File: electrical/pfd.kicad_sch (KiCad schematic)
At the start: 12 parts

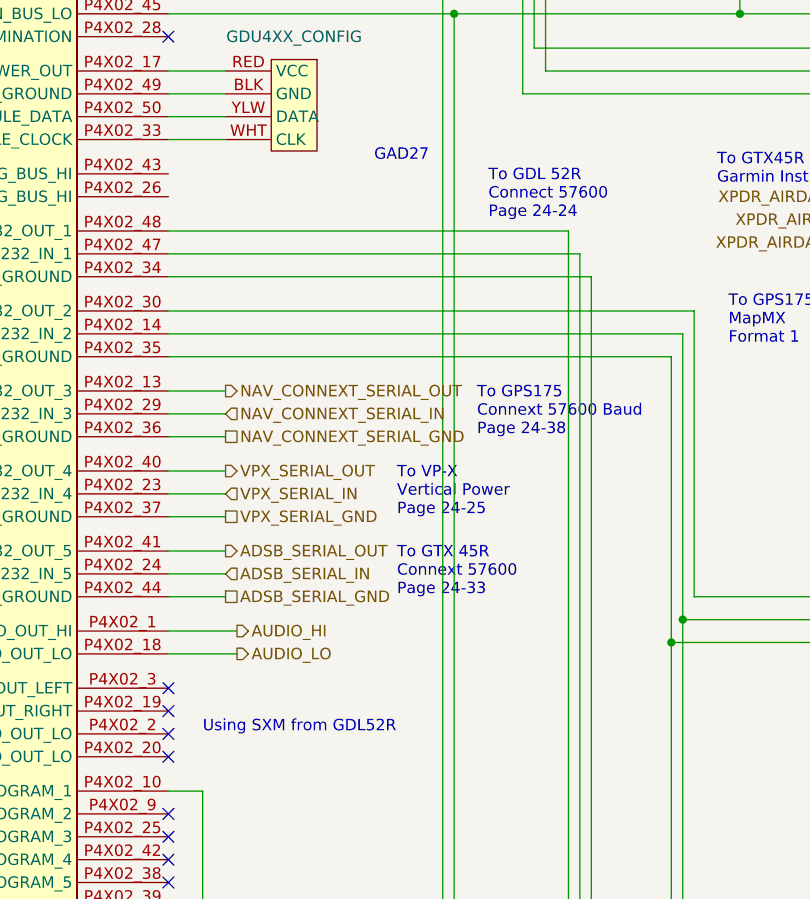
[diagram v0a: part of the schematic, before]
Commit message: Converted to breakers w/GAD 27 instead of VP-X.
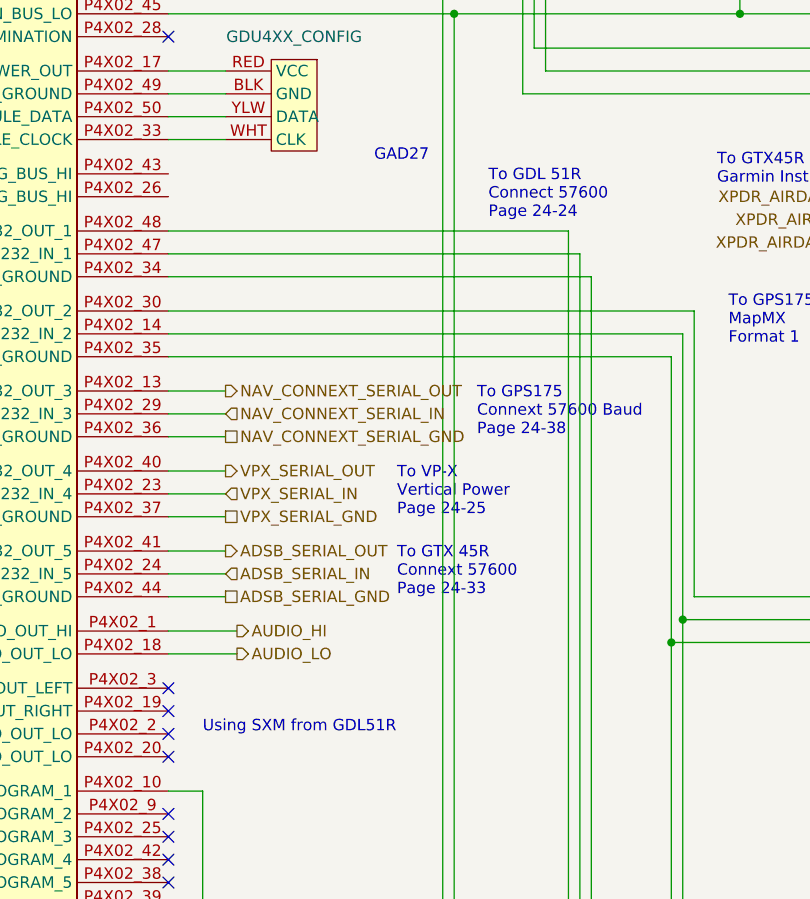
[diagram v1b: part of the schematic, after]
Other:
- note added: "To GDL 51R Connect 57600 Page 24-24"
- note added: "Using SXM from GDL51R"
- note removed: "To GDL 52R Connect 57600 Page 24-24"
- note removed: "Using SXM from GDL52R"
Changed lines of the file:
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@@
     (title "PFD & ADAHRS")
     (date "2024-02-13")
-    (rev "0.9.1")
+    (rev "1.0")
     (company "N915SN Angry Bird")
+    (comment 1 "w/Breakers")
   )
   (junction (at 151.13 212.09) (diameter 0) (color 0 0 0 0)
@@
     (effects (font (size 1.27 1.27)) (justify left bottom))
   )
-  (text "Using SXM from GDL52R" (at 66.04 142.24 0)
+  (text "Using SXM from GDL51R" (at 66.04 142.24 0)
     (effects (font (size 1.27 1.27)) (justify left bottom))
   )
@@
     (effects (font (size 1.27 1.27)) (justify left bottom))
   )
-  (text "To GDL 52R\nConnect 57600\nPage 24-24" (at 97.79 85.09 0)
-    (effects (font (size 1.27 1.27)) (justify left bottom))
-  )
+  (text "To GDL 51R\nConnect 57600\nPage 24-24" (at 97.79 85.09 0)
+    (effects (font (size 1.27 1.27)) (justify left bottom))
+  )

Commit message: Unknown set of changes. Didn't spent time to look
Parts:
- added GHA15_USB: USB_A, symbol Connector:USB_A
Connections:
- net at GHA15.10 (USBO_DM): now also GHA15_USB.2 (D-)
- net at GHA15.19 (USB_VBUS): now also GHA15_USB.1 (VBUS)
- net at GHA15.20 (SIGNAL_GROUND): now also GHA15_USB.4 (GND), GHA15_USB.5 (Shield)
- net at GHA15.9 (USBO_DP): now also GHA15_USB.3 (D+)
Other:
- moved on the sheet: G5, GHA15

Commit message: Interim check-in. Not sure what I was doing.
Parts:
- removed UAT_ANT: Antenna, symbol Device:Antenna
- renumbered GDL52R to GDL51R
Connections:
- net VPX_SERIAL_GND: no longer names the net of GDU450.P4X02_37 (SIGNAL_GROUND)
- net VPX_SERIAL_IN: no longer names the net of GDU450.P4X02_23 (RS-232_IN_4)
- net VPX_SERIAL_OUT: no longer names the net of GDU450.P4X02_40 (RS-232_OUT_4)
- no-connect marks 16 -> 18
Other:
- note removed: "To VP-X Vertical Power Page 24-25"
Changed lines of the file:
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@@
   )
   (no_connect (at 62.23 151.13))
+  (no_connect (at 63.5 234.95))
   (no_connect (at 163.83 200.66))
   (no_connect (at 154.94 35.56))
@@
   (no_connect (at 62.23 139.7))
   (no_connect (at 157.48 160.02))
+  (no_connect (at 63.5 229.87))
   (no_connect (at 62.23 137.16))
   (no_connect (at 62.23 142.24))
@@
     (stroke (width 0) (type default))
   )
-  (wire (pts (xy 63.5 234.95) (xy 64.77 234.95))
-    (stroke (width 0) (type default))
-  )
   (wire (pts (xy 109.22 91.44) (xy 109.22 208.28))
     (stroke (width 0) (type default))
@@
     (stroke (width 0) (type default))
   )
-  (wire (pts (xy 62.23 113.03) (xy 68.58 113.03))
-    (stroke (width 0) (type default))
-  )
   (wire (pts (xy 133.35 168.91) (xy 133.35 195.58))
     (stroke (width 0) (type default))
@@
     (stroke (width 0) (type default))
   )
-  (wire (pts (xy 62.23 118.11) (xy 68.58 118.11))
-    (stroke (width 0) (type default))
-  )
   (wire (pts (xy 62.23 88.9) (xy 107.95 88.9))
     (stroke (width 0) (type default))
@@
     (stroke (width 0) (type default))
   )
-  (wire (pts (xy 62.23 115.57) (xy 68.58 115.57))
-    (stroke (width 0) (type default))
-  )
   (wire (pts (xy 92.71 59.69) (xy 124.46 59.69))
     (stroke (width 0) (type default))
@@
     (stroke (width 0) (type default))
   )
-  (text "To VP-X\nVertical Power\nPage 24-25" (at 87.63 118.11 0)
-    (effects (font (size 1.27 1.27)) (justify left bottom))
+  (text_box "J251\n1 CAN H\n2 CAN L\n4 RS-232 RX-1\n5 RS-232 TX-1\n6 Ground\n7 Power 1\n8 Power 2\n9 Ground"
+    (at 185.42 116.84 0) (size 18.415 19.685)
+    (stroke (width 0) (type default))
+    (fill (type none))
+    (effects (font (size 1.27 1.27)) (justify left top))
+  )
+  (text_box "J4X01 from Zlin\n4 RS-232 RX\n5 RS-232 TX\n6 Signal Gnd"
+    (at 74.295 13.335 0) (size 17.78 9.525)
+    (stroke (width 0) (type default))
+    (fill (type none))
+    (effects (font (size 1.27 1.27)) (justify left top))
+  )
+  (text_box "J252\n 1 OAT Power\n 2 OAT High\n 3 OAT Low\n 9 RS-232 TX 3\n10 RS0232 RX 3\n11 Ground\n"
+    (at 122.555 108.585 0) (size 18.415 15.875)
+    (stroke (width 0) (type default))
+    (fill (type none))
+    (effects (font (size 1.27 1.27)) (justify left top))
+  )
+  (text_box "GDU\nRS232 1 Connext 57600\nRS232 2 Connext 57600\nRS232 3 None\nRS232 4 Garmin Instrument Data\nRS232 5 None\n\nTransponder\nRS232 2 ADS-B+ GPS Format 1\nRS232 3 Connect Format 1\nRS232 4 None"
+    (at -38.735 67.31 0) (size 34.925 24.13)
+    (stroke (width 0) (type default))
+    (fill (type none))
+    (effects (font (size 1.27 1.27)) (justify left top))
+  )
+  (text_box "J4X02 from Zlin\n 3 Stereo Out Left\n 6 Do not use\n10 CDU System ID 1\n14 RS-232 IN\n16 Power Ground\n17 Config Module Power Out\n19 Stereo Out Right\n20 Stereo Out Lo\n23 RS-232 IN 4\n30 RS-232 out 2\n31 Aircraft Power 2\n32 Aircraft Power 1\n33 Config Module Clock\n34 Signal Ground\n35 Signal Ground\n40 RS-232 Out 4\n45 Can Bus Lo\n46 Can Bus Hi\n47 RS-232 In 1\n48 RS-232 Out 1\n49 Config Module Ground\n50 Config Module Data"
+    (at 106.045 5.08 0) (size 27.305 50.165)
+    (stroke (width 0) (type default))
+    (fill (type none))
+    (effects (font (size 1.27 1.27)) (justify left top))
+  )
+  (text_box "GDL51\n 7 RS232 TX 1\n 8 RS232 RX 1\n 9 GROUND\n10 POWER\n11 SIGNAL GROUND\n13 MUSIC OUT LEFT\n14 MUSIC OUT LO\n15 MUSIC OUT RIGHT"
+    (at 17.145 236.855 0) (size 21.59 23.495)
+    (stroke (width 0) (type default))
+    (fill (type none))
+    (effects (font (size 1.27 1.27)) (justify left top))
   )
   (text "Using SXM from GDL51R" (at 66.04 142.24 0)
@@
     (effects (font (size 1.27 1.27)) (justify left))
   )
-  (hierarchical_label "VPX_SERIAL_GND" (shape passive) (at 68.58 118.11 0) (fields_autoplaced)
-    (effects (font (size 1.27 1.27)) (justify left))
-  )
   (hierarchical_label "XPDR_AIRDATA_SERIAL_OUT" (shape output) (at 149.86 82.55 180) (fields_autoplaced)
     (effects (font (size 1.27 1.27)) (justify right))
@@
     (effects (font (size 1.27 1.27)) (justify right))
   )
-  (hierarchical_label "VPX_SERIAL_IN" (shape input) (at 68.58 115.57 0) (fields_autoplaced)
-    (effects (font (size 1.27 1.27)) (justify left))
-  )
   (hierarchical_label "NAV_CONNEXT_SERIAL_IN" (shape input) (at 68.58 106.68 0) (fields_autoplaced)
     (effects (font (size 1.27 1.27)) (justify left))
@@
   (hierarchical_label "XPDR_AIRDATA_SERIAL_IN" (shape input) (at 149.86 85.09 180) (fields_autoplaced)
     (effects (font (size 1.27 1.27)) (justify right))
-  )
-  (hierarchical_label "VPX_SERIAL_OUT" (shape output) (at 68.58 113.03 0) (fields_autoplaced)
-    (effects (font (size 1.27 1.27)) (justify left))
   )
   (hierarchical_label "G5_BAK_PWR" (shape input) (at 151.13 153.67 180) (fields_autoplaced)
@@
   (symbol (lib_id "flyerx:Garmin_GDL52R") (at 30.48 193.04 0) (unit 1)
     (in_bom yes) (on_board yes) (dnp no) (fields_autoplaced)
-    (property "Reference" "GDL52R" (at 41.91 190.5 0)
+    (property "Reference" "GDL51R" (at 41.91 190.5 0)
       (effects (font (size 1.27 1.27)))
     )
@@
       (project "electrical"
         (path "/e8ec215a-dbe2-4eba-a577-e50a0a128049/633b5331-dc3f-449e-8212-24f89753723c"
-          (reference "GDL52R") (unit 1)
+          (reference "GDL51R") (unit 1)
         )
       )
@@
         )
       )
-    )
-  )
-  (symbol (lib_id "Device:Antenna") (at 69.85 234.95 270) (unit 1)
-    (in_bom yes) (on_board yes) (dnp no) (fields_autoplaced)
-    (property "Reference" "UAT_ANT" (at 73.66 234.95 90)
-      (effects (font (size 1.27 1.27)) (justify left))
-    )
-    (property "Value" "Antenna" (at 73.66 236.22 90)
-      (effects (font (size 1.27 1.27)) (justify left) hide)
-    )
-    (property "Footprint" "" (at 69.85 234.95 0)
-      (effects (font (size 1.27 1.27)) hide)
-    )
-    (property "Datasheet" "~" (at 69.85 234.95 0)
-      (effects (font (size 1.27 1.27)) hide)
-    )
-    (pin "1")
-    (instances
-      (project "electrical"
-        (path "/e8ec215a-dbe2-4eba-a577-e50a0a128049/633b5331-dc3f-449e-8212-24f89753723c"
-          (reference "UAT_ANT") (unit 1)
-        )
-      )

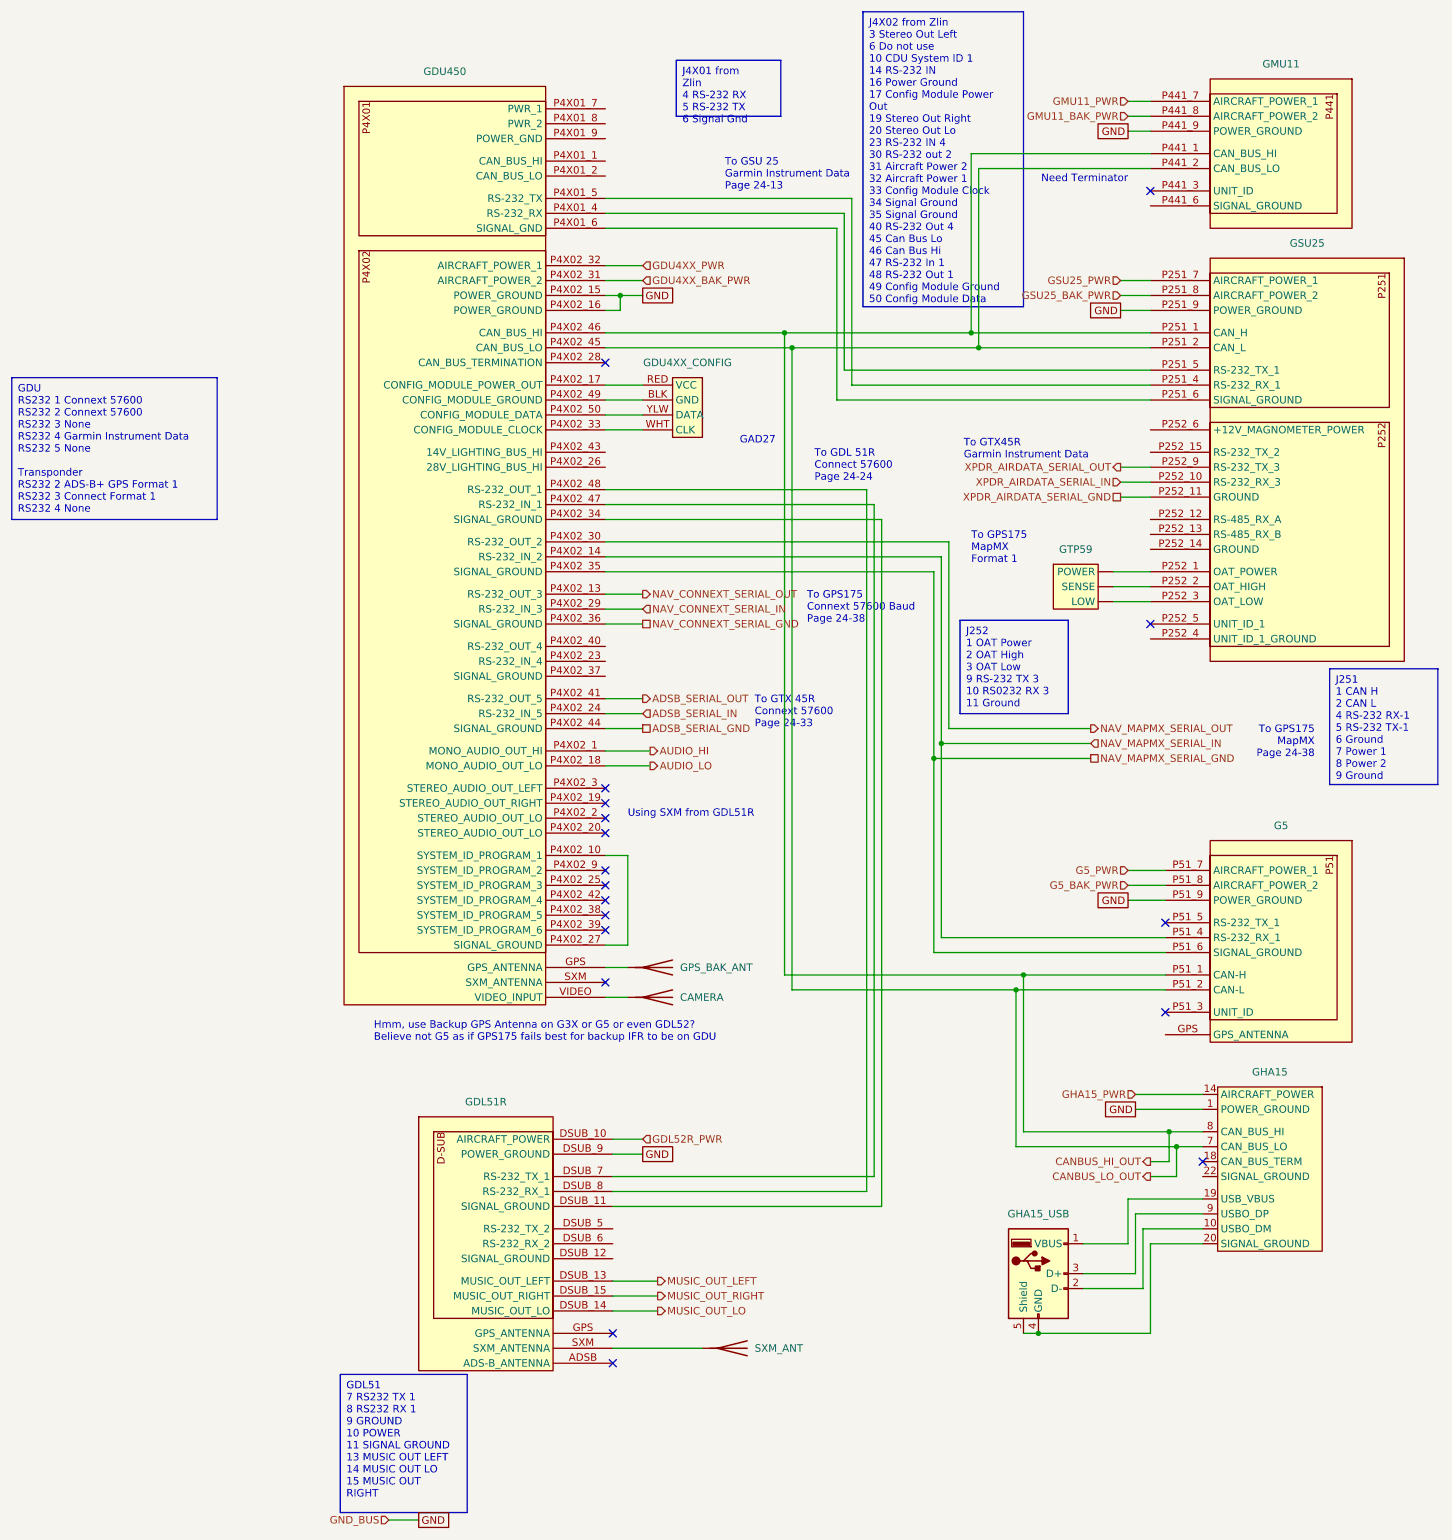
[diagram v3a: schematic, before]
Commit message: Cleaned up power and smoke.
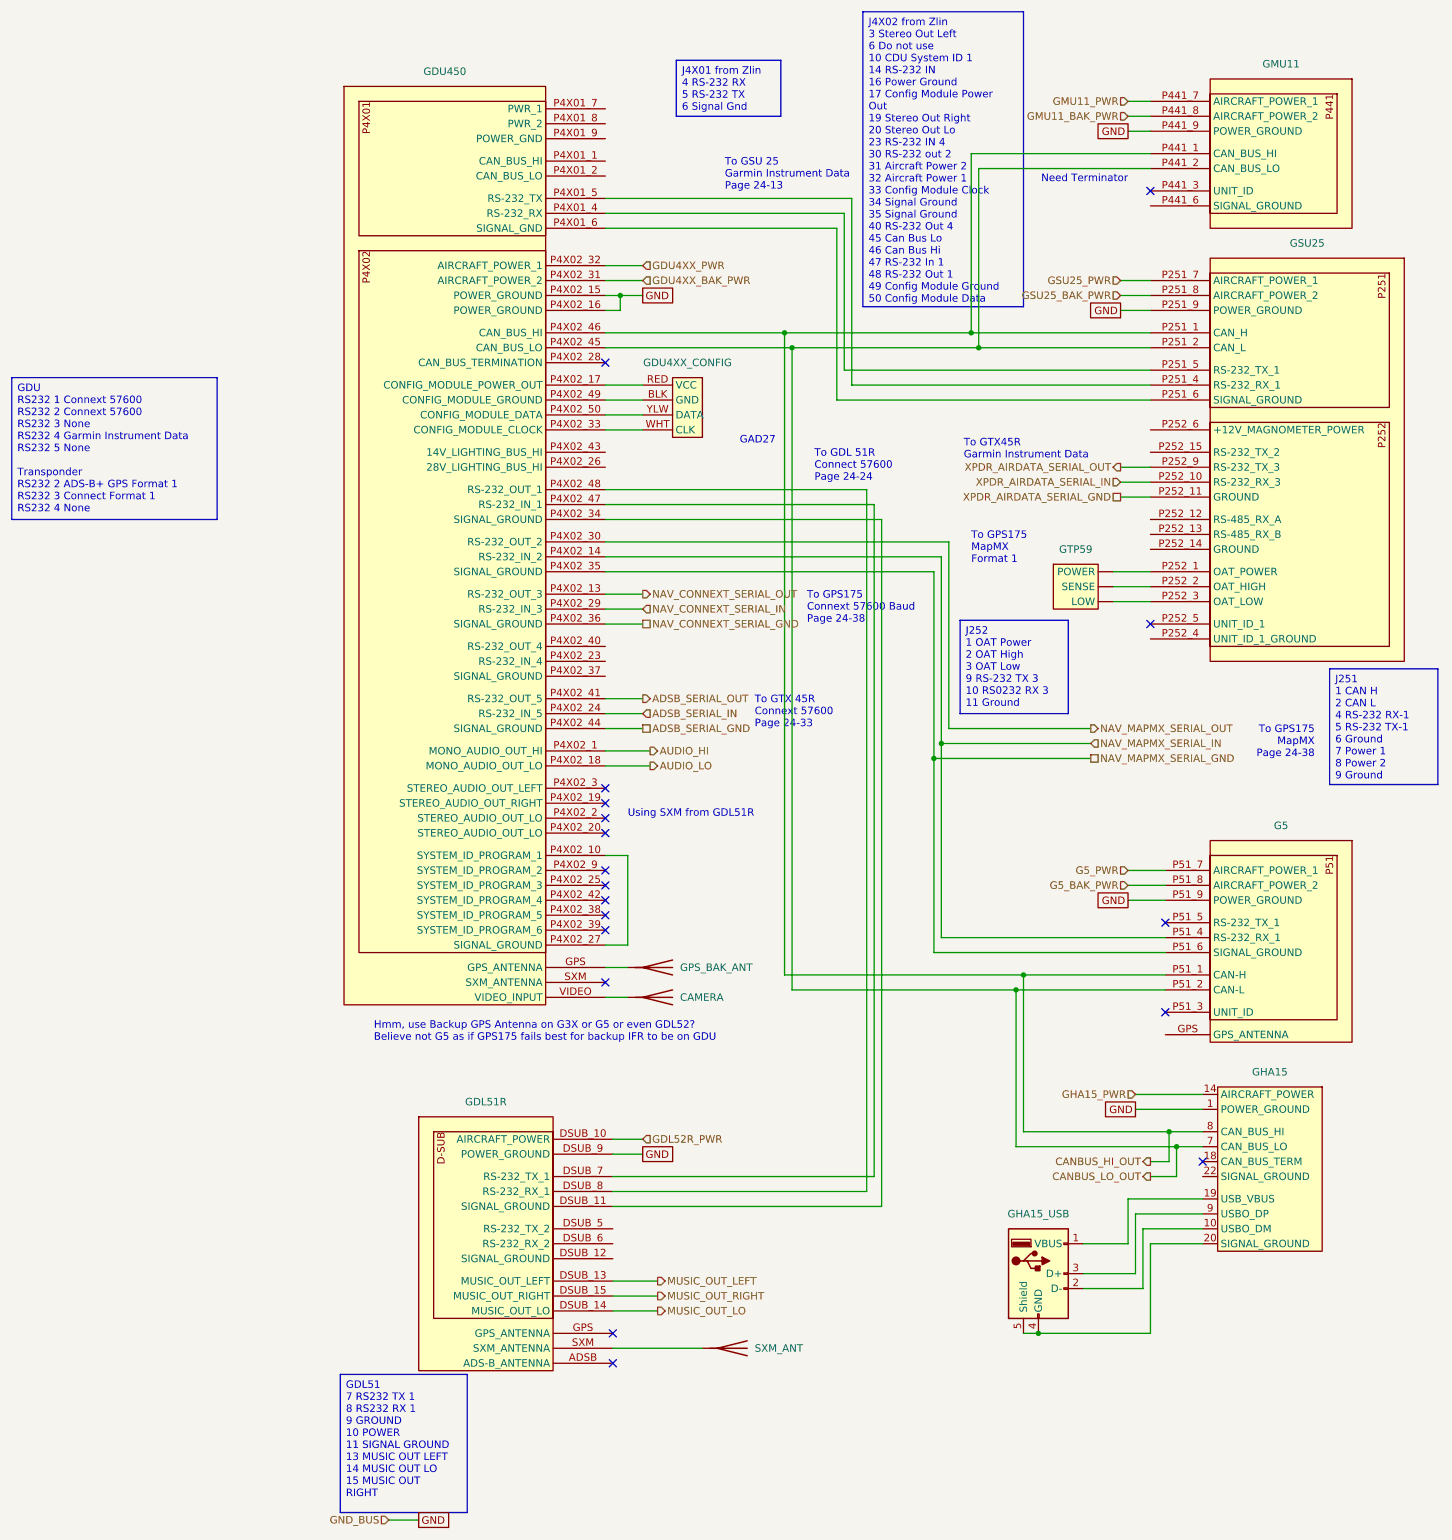
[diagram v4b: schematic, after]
